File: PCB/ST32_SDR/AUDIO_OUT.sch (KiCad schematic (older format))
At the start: 36 parts, among them J1 MIC_PTT, J3 Audio-Jack-3_2Switches, J4 LINEIN, K1 FRT5, K2 FRT5, Q1 Q_NPN_BEC, Q2 Q_NPN_BEC, U16 WM8731_alt

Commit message: UI PCB linux 1
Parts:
- C18, C20: footprint (none) -> UI:C_1206_0603
- K1, K2: footprint Relays_ThroughHole:Relay_DPDT_FRT5 -> UI:Relay_G6K-2F
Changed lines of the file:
@@
 LIBS:4ms-ic
 LIBS:Display
-LIBS:switches
-LIBS:cmos4000
+LIBS:Connector
+LIBS:Relay
 LIBS:LCSDR-cache
 EELAYER 25 0
@@
 $EndComp
 $Comp
-L GND #PWR08
+L GND #PWR013
 U 1 1 5DD2681A
 P 9000 2450
-F 0 "#PWR08" H 9000 2200 50  0001 C CNN
+F 0 "#PWR013" H 9000 2200 50  0001 C CNN
 F 1 "GND" H 9000 2300 50  0001 C CNN
 F 2 "" H 9000 2450 50  0001 C CNN
@@
 	7200 2900 7500 2900
 $Comp
-L GND #PWR09
+L GND #PWR014
 U 1 1 5DD26DA0
 P 6200 4200
-F 0 "#PWR09" H 6200 3950 50  0001 C CNN
+F 0 "#PWR014" H 6200 3950 50  0001 C CNN
 F 1 "GND" H 6200 4050 50  0001 C CNN
 F 2 "" H 6200 4200 50  0001 C CNN
@@
 Connection ~ 9000 1300
 $Comp
-L GND #PWR010
+L GND #PWR015
 U 1 1 5DD27D3B
 P 8900 1500
-F 0 "#PWR010" H 8900 1250 50  0001 C CNN
+F 0 "#PWR015" H 8900 1250 50  0001 C CNN
 F 1 "GND" H 8900 1350 50  0001 C CNN
 F 2 "" H 8900 1500 50  0001 C CNN
@@
 $EndComp
 $Comp
-L GND #PWR011
+L GND #PWR016
 U 1 1 5DD2888E
 P 7500 1400
-F 0 "#PWR011" H 7500 1150 50  0001 C CNN
+F 0 "#PWR016" H 7500 1150 50  0001 C CNN
 F 1 "GND" H 7500 1250 50  0001 C CNN
 F 2 "" H 7500 1400 50  0001 C CNN
@@
 $EndComp
 $Comp
-L GND #PWR012
+L GND #PWR017
 U 1 1 5DD288DB
 P 7500 1700
-F 0 "#PWR012" H 7500 1450 50  0001 C CNN
+F 0 "#PWR017" H 7500 1450 50  0001 C CNN
 F 1 "GND" H 7500 1550 50  0001 C CNN
 F 2 "" H 7500 1700 50  0001 C CNN
@@
 	6200 1350 7100 1350
 $Comp
-L GND #PWR013
+L GND #PWR018
 U 1 1 5DD292E5
 P 6650 1600
-F 0 "#PWR013" H 6650 1350 50  0001 C CNN
+F 0 "#PWR018" H 6650 1350 50  0001 C CNN
 F 1 "GND" H 6650 1450 50  0001 C CNN
 F 2 "" H 6650 1600 50  0001 C CNN
@@
 	6200 1350 6200 1400
 $Comp
-L GND #PWR014
+L GND #PWR019
 U 1 1 5DD29619
 P 6200 1600
-F 0 "#PWR014" H 6200 1350 50  0001 C CNN
+F 0 "#PWR019" H 6200 1350 50  0001 C CNN
 F 1 "GND" H 6200 1450 50  0001 C CNN
 F 2 "" H 6200 1600 50  0001 C CNN
@@
 Connection ~ 9300 1500
 $Comp
-L GND #PWR015
+L GND #PWR020
 U 1 1 5DD2B06D
 P 1500 4550
-F 0 "#PWR015" H 1500 4300 50  0001 C CNN
+F 0 "#PWR020" H 1500 4300 50  0001 C CNN
 F 1 "GND" H 1500 4400 50  0001 C CNN
 F 2 "" H 1500 4550 50  0001 C CNN
@@
 I2S_SDI
 $Comp
-L +3V3 #PWR016
+L +3V3 #PWR021
 U 1 1 5DDD5336
 P 7300 900
-F 0 "#PWR016" H 7300 750 50  0001 C CNN
+F 0 "#PWR021" H 7300 750 50  0001 C CNN
 F 1 "+3V3" H 7300 1040 50  0000 C CNN
 F 2 "" H 7300 900 50  0001 C CNN
@@
 $EndComp
 $Comp
-L +3V3 #PWR017
+L +3V3 #PWR022
 U 1 1 5DDD54CE
 P 9000 850
-F 0 "#PWR017" H 9000 700 50  0001 C CNN
+F 0 "#PWR022" H 9000 700 50  0001 C CNN
 F 1 "+3V3" H 9000 990 50  0000 C CNN
 F 2 "" H 9000 850 50  0001 C CNN
@@
 $EndComp
 $Comp
-L +3V3 #PWR018
+L +3V3 #PWR023
 U 1 1 5DDD554D
 P 9300 1450
-F 0 "#PWR018" H 9300 1300 50  0001 C CNN
+F 0 "#PWR023" H 9300 1300 50  0001 C CNN
 F 1 "+3V3" H 9300 1590 50  0000 C CNN
 F 2 "" H 9300 1450 50  0001 C CNN
@@
 	6850 2600 7500 2600
 $Comp
-L GND #PWR019
+L GND #PWR024
 U 1 1 5DDD5FC7
 P 2000 4750
-F 0 "#PWR019" H 2000 4500 50  0001 C CNN
+F 0 "#PWR024" H 2000 4500 50  0001 C CNN
 F 1 "GND" H 2000 4600 50  0001 C CNN
 F 2 "" H 2000 4750 50  0001 C CNN
@@
 Q_OUT
 $Comp
-L GND #PWR020
+L GND #PWR025
 U 1 1 5DDEB3C2
 P 1300 6250
-F 0 "#PWR020" H 1300 6000 50  0001 C CNN
+F 0 "#PWR025" H 1300 6000 50  0001 C CNN
 F 1 "GND" H 1300 6100 50  0001 C CNN
 F 2 "" H 1300 6250 50  0001 C CNN
@@
 F 0 "C20" V 7700 3950 50  0000 L CNN
 F 1 "1nF" V 7600 3900 50  0000 L CNN
-F 2 "" H 7500 4000 50  0001 C CNN
+F 2 "UI:C_1206_0603" H 7500 4000 50  0001 C CNN
 F 3 "" H 7500 4000 50  0001 C CNN
 	1    7500 4000
@@
 F 0 "C18" H 7350 4350 50  0000 L CNN
 F 1 "1nF" H 7350 4250 50  0000 L CNN
-F 2 "" H 7200 4300 50  0001 C CNN
+F 2 "UI:C_1206_0603" H 7200 4300 50  0001 C CNN
 F 3 "" H 7200 4300 50  0001 C CNN
 	1    7200 4300
@@
 Connection ~ 7200 3900
 $Comp
-L GND #PWR021
+L GND #PWR026
 U 1 1 5DDE20EC
 P 7200 4400
-F 0 "#PWR021" H 7200 4150 50  0001 C CNN
+F 0 "#PWR026" H 7200 4150 50  0001 C CNN
 F 1 "GND" H 7200 4250 50  0001 C CNN
 F 2 "" H 7200 4400 50  0001 C CNN
@@
 $EndComp
 $Comp
-L GND #PWR022
+L GND #PWR027
 U 1 1 5DDE216C
 P 7600 4000
-F 0 "#PWR022" H 7600 3750 50  0001 C CNN
+F 0 "#PWR027" H 7600 3750 50  0001 C CNN
 F 1 "GND" H 7600 3850 50  0001 C CNN
 F 2 "" H 7600 4000 50  0001 C CNN
@@
 Connection ~ 2450 3300
 $Comp
-L GND #PWR023
+L GND #PWR028
 U 1 1 5DDEC497
 P 2450 3600
-F 0 "#PWR023" H 2450 3350 50  0001 C CNN
+F 0 "#PWR028" H 2450 3350 50  0001 C CNN
 F 1 "GND" H 2450 3450 50  0001 C CNN
 F 2 "" H 2450 3600 50  0001 C CNN
@@
 	2000 3600 2000 3300
 $Comp
-L +3V3 #PWR024
+L +3V3 #PWR029
 U 1 1 5DDECF82
 P 2250 3000
-F 0 "#PWR024" H 2250 2850 50  0001 C CNN
+F 0 "#PWR029" H 2250 2850 50  0001 C CNN
 F 1 "+3V3" H 2250 3140 50  0000 C CNN
 F 2 "" H 2250 3000 50  0001 C CNN
@@
 $EndComp
 $Comp
-L GND #PWR025
+L GND #PWR030
 U 1 1 5DDFCD99
 P 6900 950
-F 0 "#PWR025" H 6900 700 50  0001 C CNN
+F 0 "#PWR030" H 6900 700 50  0001 C CNN
 F 1 "GND" H 6900 800 50  0001 C CNN
 F 2 "" H 6900 950 50  0001 C CNN
@@
 Connection ~ 9000 900
 $Comp
-L GND #PWR026
+L GND #PWR031
 U 1 1 5DDFD5D6
 P 9450 900
-F 0 "#PWR026" H 9450 650 50  0001 C CNN
+F 0 "#PWR031" H 9450 650 50  0001 C CNN
 F 1 "GND" H 9450 750 50  0001 C CNN
 F 2 "" H 9450 900 50  0001 C CNN
@@
 F 0 "K1" H 3450 6500 50  0000 L CNN
 F 1 "FRT5" H 3450 6400 50  0000 L CNN
-F 2 "Relays_ThroughHole:Relay_DPDT_FRT5" H 3350 6400 50  0001 C CNN
+F 2 "UI:Relay_G6K-2F" H 3350 6400 50  0001 C CNN
 F 3 "" H 3450 6500 50  0001 C CNN
 	1    2600 6350
@@
 	1800 5850 1700 5850
 $Comp
-L GND #PWR027
+L GND #PWR032
 U 1 1 5DE0CE18
 P 4050 7100
-F 0 "#PWR027" H 4050 6850 50  0001 C CNN
+F 0 "#PWR032" H 4050 6850 50  0001 C CNN
 F 1 "GND" H 4050 6950 50  0001 C CNN
 F 2 "" H 4050 7100 50  0001 C CNN
@@
 Connection ~ 3100 6550
 $Comp
-L GND #PWR028
+L GND #PWR033
 U 1 1 5DE0D073
 P 3100 6850
-F 0 "#PWR028" H 3100 6600 50  0001 C CNN
+F 0 "#PWR033" H 3100 6600 50  0001 C CNN
 F 1 "GND" H 3100 6700 50  0001 C CNN
 F 2 "" H 3100 6850 50  0001 C CNN
@@
 $EndComp
 $Comp
-L GND #PWR029
+L GND #PWR034
 U 1 1 5DE0DDB8
 P 4500 7150
-F 0 "#PWR029" H 4500 6900 50  0001 C CNN
+F 0 "#PWR034" H 4500 6900 50  0001 C CNN
 F 1 "GND" H 4500 7000 50  0001 C CNN
 F 2 "" H 4500 7150 50  0001 C CNN
@@
 	5000 6900 5100 6900
 $Comp
-L +12V #PWR030
+L +12V #PWR035
 U 1 1 5DE0E43B
 P 1850 6550
-F 0 "#PWR030" H 1850 6400 50  0001 C CNN
+F 0 "#PWR035" H 1850 6400 50  0001 C CNN
 F 1 "+12V" V 1850 6800 50  0000 C CNN
 F 2 "" H 1850 6550 50  0001 C CNN
@@
 F 0 "K2" H 3250 2050 50  0000 L CNN
 F 1 "FRT5" H 3250 1950 50  0000 L CNN
-F 2 "Relays_ThroughHole:Relay_DPDT_FRT5" H 3150 1950 50  0001 C CNN
+F 2 "UI:Relay_G6K-2F" H 3150 1950 50  0001 C CNN
 F 3 "" H 3250 2050 50  0001 C CNN
 	1    2400 1900
@@
 $EndComp
 $Comp
-L GND #PWR031
+L GND #PWR036
 U 1 1 5DE10A90
 P 3850 2650
-F 0 "#PWR031" H 3850 2400 50  0001 C CNN
+F 0 "#PWR036" H 3850 2400 50  0001 C CNN
 F 1 "GND" H 3850 2500 50  0001 C CNN
 F 2 "" H 3850 2650 50  0001 C CNN
@@
 Connection ~ 2900 2100
 $Comp
-L GND #PWR032
+L GND #PWR037
 U 1 1 5DE10A9A
 P 2900 2400
-F 0 "#PWR032" H 2900 2150 50  0001 C CNN
+F 0 "#PWR037" H 2900 2150 50  0001 C CNN
 F 1 "GND" H 2900 2250 50  0001 C CNN
 F 2 "" H 2900 2400 50  0001 C CNN
@@
 $EndComp
 $Comp
-L GND #PWR033
+L GND #PWR038
 U 1 1 5DE10AB9
 P 4300 2700
-F 0 "#PWR033" H 4300 2450 50  0001 C CNN
+F 0 "#PWR038" H 4300 2450 50  0001 C CNN
 F 1 "GND" H 4300 2550 50  0001 C CNN
 F 2 "" H 4300 2700 50  0001 C CNN
@@
 	4800 2450 4900 2450
 $Comp
-L +12V #PWR034
+L +12V #PWR039
 U 1 1 5DE10AC2
 P 1650 2100
-F 0 "#PWR034" H 1650 1950 50  0001 C CNN
+F 0 "#PWR039" H 1650 1950 50  0001 C CNN
 F 1 "+12V" V 1650 2350 50  0000 C CNN
 F 2 "" H 1650 2100 50  0001 C CNN

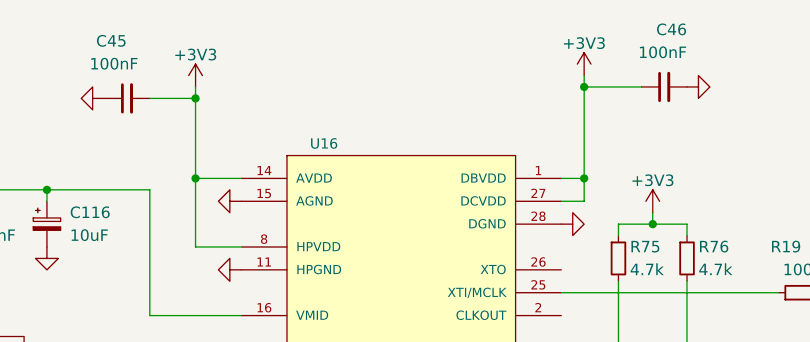
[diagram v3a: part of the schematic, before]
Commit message: PCB Linux 2, update AUDIO_OUT
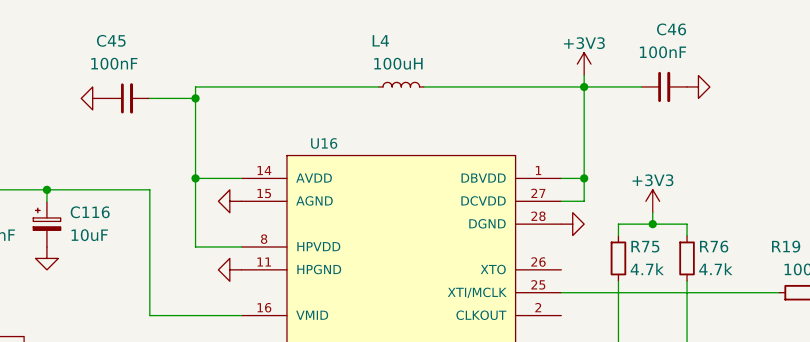
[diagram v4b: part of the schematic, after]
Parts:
- added L4: 100uH, Choke_Axial_ThroughHole:Choke_Horizontal_RM10mm, symbol L_Small
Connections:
- net +3V3: now also L4.2; no longer C45.2, U16.14 (AVDD), U16.8 (HPVDD)
- new net: C45.2, L4.1, U16.14 (AVDD), U16.8 (HPVDD)
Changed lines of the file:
@@
 LIBS:4ms-ic
 LIBS:Display
-LIBS:switches
-LIBS:cmos4000
+LIBS:Connector
+LIBS:Relay
 LIBS:LCSDR-cache
 EELAYER 25 0
@@
 $EndComp
 $Comp
-L GND #PWR013
+L GND #PWR014
 U 1 1 5DD2681A
 P 9000 2450
-F 0 "#PWR013" H 9000 2200 50  0001 C CNN
+F 0 "#PWR014" H 9000 2200 50  0001 C CNN
 F 1 "GND" H 9000 2300 50  0001 C CNN
 F 2 "" H 9000 2450 50  0001 C CNN
@@
 	7200 2900 7500 2900
 $Comp
-L GND #PWR014
+L GND #PWR015
 U 1 1 5DD26DA0
 P 6200 4200
-F 0 "#PWR014" H 6200 3950 50  0001 C CNN
+F 0 "#PWR015" H 6200 3950 50  0001 C CNN
 F 1 "GND" H 6200 4050 50  0001 C CNN
 F 2 "" H 6200 4200 50  0001 C CNN
@@
 Connection ~ 9000 1300
 $Comp
-L GND #PWR015
+L GND #PWR016
 U 1 1 5DD27D3B
 P 8900 1500
-F 0 "#PWR015" H 8900 1250 50  0001 C CNN
+F 0 "#PWR016" H 8900 1250 50  0001 C CNN
 F 1 "GND" H 8900 1350 50  0001 C CNN
 F 2 "" H 8900 1500 50  0001 C CNN
@@
 $EndComp
 $Comp
-L GND #PWR016
+L GND #PWR017
 U 1 1 5DD2888E
 P 7500 1400
-F 0 "#PWR016" H 7500 1150 50  0001 C CNN
+F 0 "#PWR017" H 7500 1150 50  0001 C CNN
 F 1 "GND" H 7500 1250 50  0001 C CNN
 F 2 "" H 7500 1400 50  0001 C CNN
@@
 $EndComp
 $Comp
-L GND #PWR017
+L GND #PWR018
 U 1 1 5DD288DB
 P 7500 1700
-F 0 "#PWR017" H 7500 1450 50  0001 C CNN
+F 0 "#PWR018" H 7500 1450 50  0001 C CNN
 F 1 "GND" H 7500 1550 50  0001 C CNN
 F 2 "" H 7500 1700 50  0001 C CNN
@@
 	6200 1350 7100 1350
 $Comp
-L GND #PWR018
+L GND #PWR019
 U 1 1 5DD292E5
 P 6650 1600
-F 0 "#PWR018" H 6650 1350 50  0001 C CNN
+F 0 "#PWR019" H 6650 1350 50  0001 C CNN
 F 1 "GND" H 6650 1450 50  0001 C CNN
 F 2 "" H 6650 1600 50  0001 C CNN
@@
 	6200 1350 6200 1400
 $Comp
-L GND #PWR019
+L GND #PWR020
 U 1 1 5DD29619
 P 6200 1600
-F 0 "#PWR019" H 6200 1350 50  0001 C CNN
+F 0 "#PWR020" H 6200 1350 50  0001 C CNN
 F 1 "GND" H 6200 1450 50  0001 C CNN
 F 2 "" H 6200 1600 50  0001 C CNN
@@
 Connection ~ 9300 1500
 $Comp
-L GND #PWR020
+L GND #PWR021
 U 1 1 5DD2B06D
 P 1500 4550
-F 0 "#PWR020" H 1500 4300 50  0001 C CNN
+F 0 "#PWR021" H 1500 4300 50  0001 C CNN
 F 1 "GND" H 1500 4400 50  0001 C CNN
 F 2 "" H 1500 4550 50  0001 C CNN
@@
 I2S_SDI
 $Comp
-L +3V3 #PWR021
-U 1 1 5DDD5336
-P 7300 900
-F 0 "#PWR021" H 7300 750 50  0001 C CNN
-F 1 "+3V3" H 7300 1040 50  0000 C CNN
-F 2 "" H 7300 900 50  0001 C CNN
-F 3 "" H 7300 900 50  0001 C CNN
-	1    7300 900
-	1    0    0    -1
-$EndComp
-$Comp
 L +3V3 #PWR022
 U 1 1 5DDD54CE
@@
 $EndComp
 Wire Wire Line
-	9000 900  9250 900
+	8300 900  9250 900
 Connection ~ 9000 900
 $Comp
@@
 Text GLabel 5100 6900 2    60   Input ~ 0
 TX2
+$Comp
+L L_Small L4
+U 1 1 5DE4E198
+P 8200 900
+F 0 "L4" V 8400 950 50  0000 L CNN
+F 1 "100uH" V 8300 800 50  0000 L CNN
+F 2 "Choke_Axial_ThroughHole:Choke_Horizontal_RM10mm" H 8200 900 50  0001 C CNN
+F 3 "" H 8200 900 50  0001 C CNN
+	1    8200 900
+	0    -1   -1   0
+$EndComp
+Wire Wire Line
+	7300 900  8100 900
 $EndSCHEMATC
